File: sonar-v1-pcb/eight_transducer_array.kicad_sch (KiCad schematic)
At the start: 1 part, among them U1 ADS8568SPM

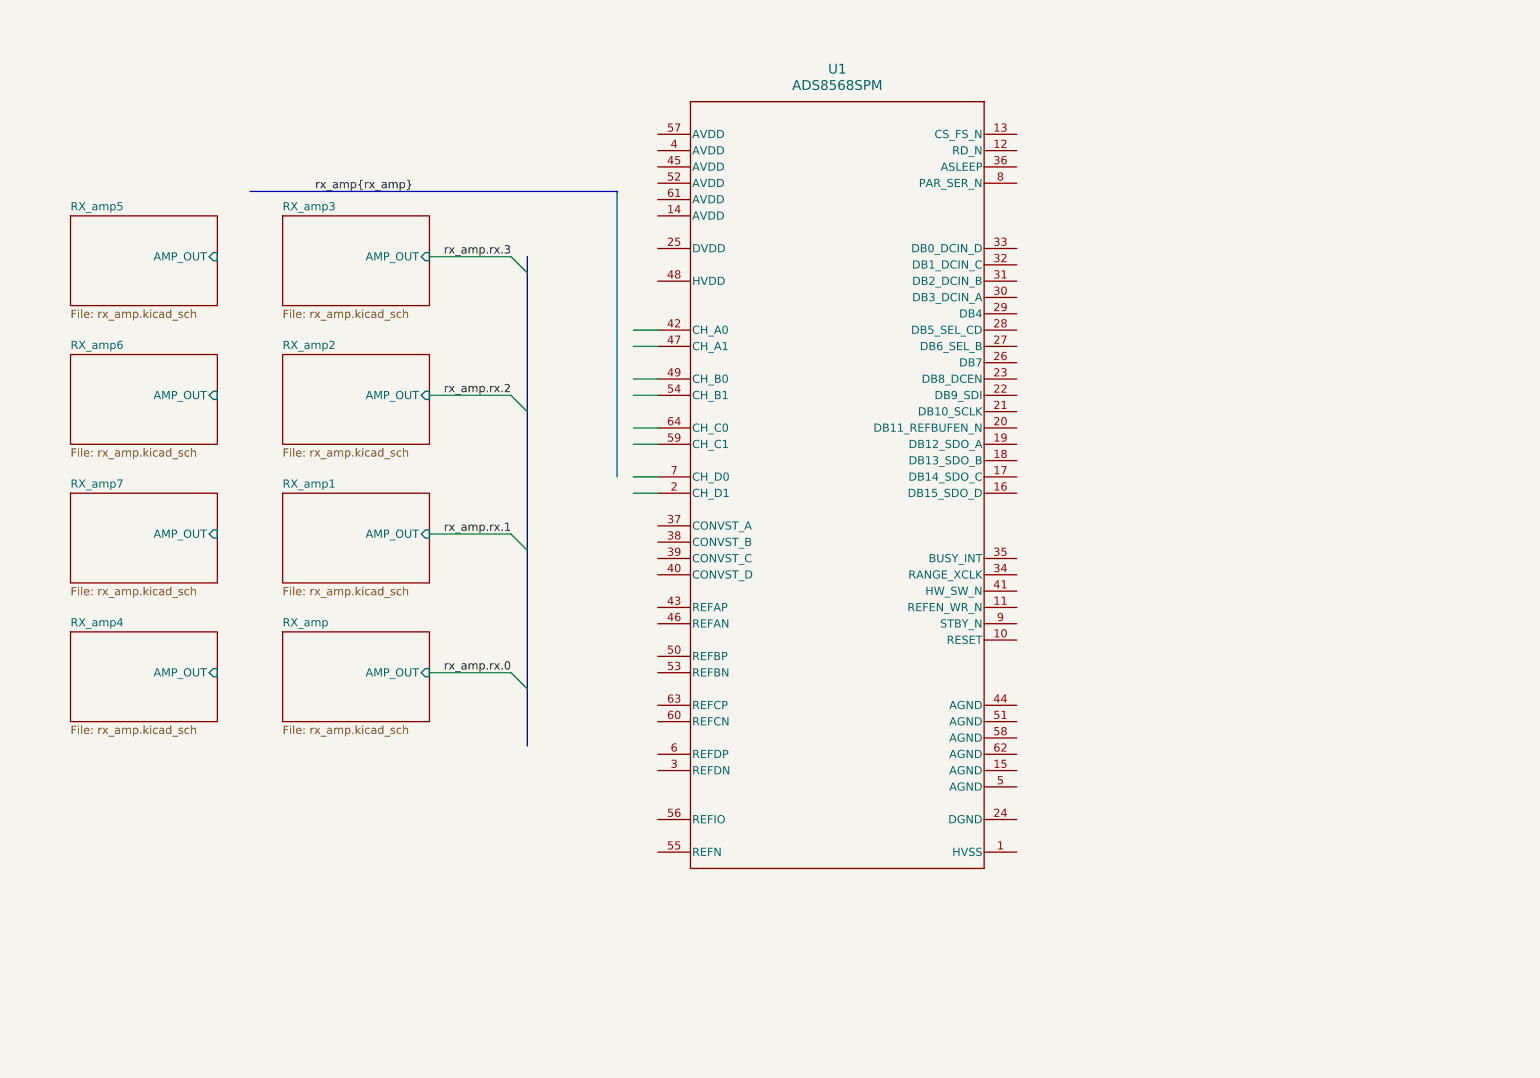
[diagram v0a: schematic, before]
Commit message: Update gitignore and save schematic/PCB progress
Co-Authored-By: Claude Opus 4.6 <noreply@anthropic.com>
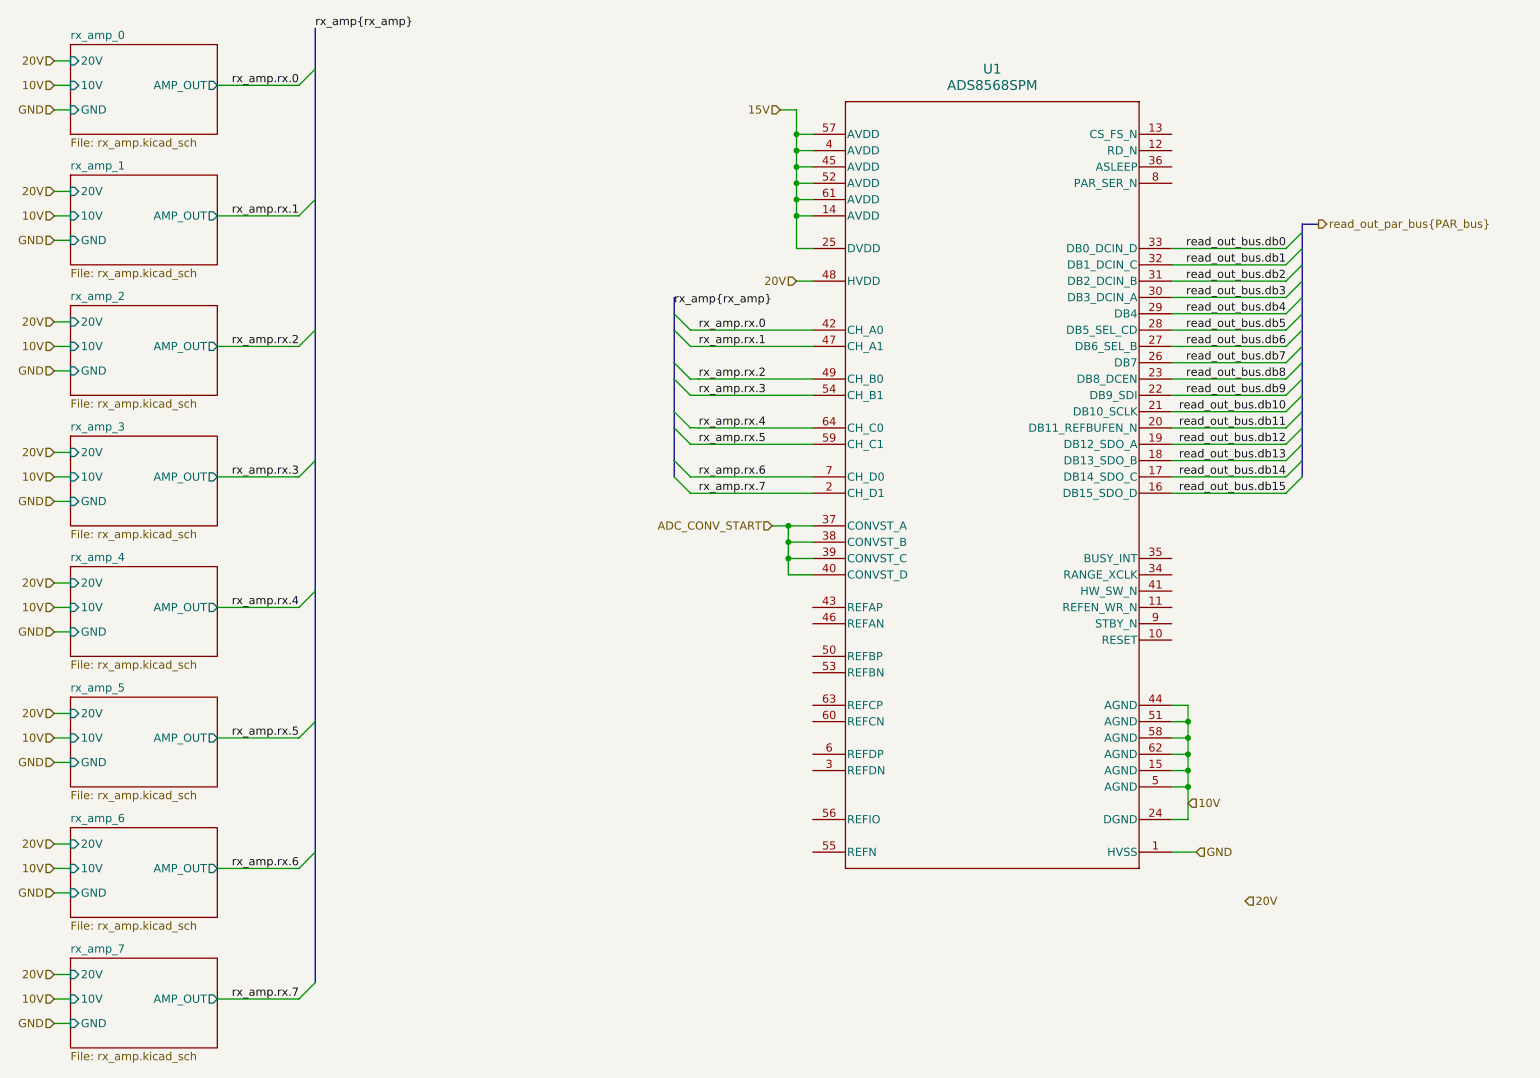
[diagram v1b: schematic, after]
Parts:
- U1: footprint PM0064A-IPC_A -> Package_QFP:LQFP-64-1EP_10x10mm_P0.5mm_EP6.5x6.5mm_ThermalVias
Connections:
- net rx_amp.rx.0: now also U1.42 (CH_A0)
- net rx_amp.rx.1: now also U1.47 (CH_A1)
- net rx_amp.rx.2: now also U1.49 (CH_B0)
- net rx_amp.rx.3: now also U1.54 (CH_B1)
- net GND: now reaches U1.1 (HVSS)
- net 15V: now reaches U1.14 (AVDD)
- net 15V: now also U1.25 (DVDD), U1.4 (AVDD), U1.45 (AVDD), U1.52 (AVDD), U1.57 (AVDD), U1.61 (AVDD)
- net 10V: now reaches U1.15 (AGND)
- net 10V: now also U1.24 (DGND), U1.44 (AGND), U1.5 (AGND), U1.51 (AGND), U1.58 (AGND), U1.62 (AGND)
- net read_out_bus.db15: now reaches U1.16 (DB15_SDO_D)
- net read_out_bus.db14: now reaches U1.17 (DB14_SDO_C)
- net read_out_bus.db13: now reaches U1.18 (DB13_SDO_B)
- net read_out_bus.db12: now reaches U1.19 (DB12_SDO_A)
- net rx_amp.rx.7: now reaches U1.2 (CH_D1)
- net read_out_bus.db11: now reaches U1.20 (DB11_REFBUFEN_N)
- net read_out_bus.db10: now reaches U1.21 (DB10_SCLK)
- net read_out_bus.db9: now reaches U1.22 (DB9_SDI)
- net read_out_bus.db8: now reaches U1.23 (DB8_DCEN)
- net read_out_bus.db7: now reaches U1.26 (DB7)
- net read_out_bus.db6: now reaches U1.27 (DB6_SEL_B)
- net read_out_bus.db5: now reaches U1.28 (DB5_SEL_CD)
- net read_out_bus.db4: now reaches U1.29 (DB4)
- net read_out_bus.db3: now reaches U1.30 (DB3_DCIN_A)
- net read_out_bus.db2: now reaches U1.31 (DB2_DCIN_B)
- net read_out_bus.db1: now reaches U1.32 (DB1_DCIN_C)
- net read_out_bus.db0: now reaches U1.33 (DB0_DCIN_D)
- net ADC_CONV_START: now reaches U1.37 (CONVST_A)
- net ADC_CONV_START: now also U1.38 (CONVST_B), U1.39 (CONVST_C), U1.40 (CONVST_D)
- net 20V: now reaches U1.48 (HVDD)
- net rx_amp.rx.5: now reaches U1.59 (CH_C1)
- net rx_amp.rx.4: now reaches U1.64 (CH_C0)
- net rx_amp.rx.6: now reaches U1.7 (CH_D0)
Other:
- sheet RX_amp3 renamed rx_amp_0
- removed sheet RX_amp
- removed sheet RX_amp1
- removed sheet RX_amp2
- removed sheet RX_amp4
- removed sheet RX_amp5
- removed sheet RX_amp6
- removed sheet RX_amp7
- added sheet rx_amp_1 (rx_amp.kicad_sch)
- added sheet rx_amp_2 (rx_amp.kicad_sch)
- added sheet rx_amp_3 (rx_amp.kicad_sch)
- added sheet rx_amp_4 (rx_amp.kicad_sch)
- added sheet rx_amp_5 (rx_amp.kicad_sch)
- added sheet rx_amp_6 (rx_amp.kicad_sch)
- added sheet rx_amp_7 (rx_amp.kicad_sch)
- sheet rx_amp_0 ports: added 10V, 20V, GND; removed none
- moved on the sheet: U1
